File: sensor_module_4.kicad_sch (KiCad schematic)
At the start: 26 parts, among them J1 Conn_Coaxial, J3 Conn_Coaxial, J4 Conn_Coaxial, J5 Conn_Coaxial, U12 REF3025, U13 MCP3204, U16 INA333xxDGK, U17 INA333xxDGK, U18 INA333xxDGK, U19 INA333xxDGK, U6 M24C02-WMN, U7 TPS22929D, U8 REF3040

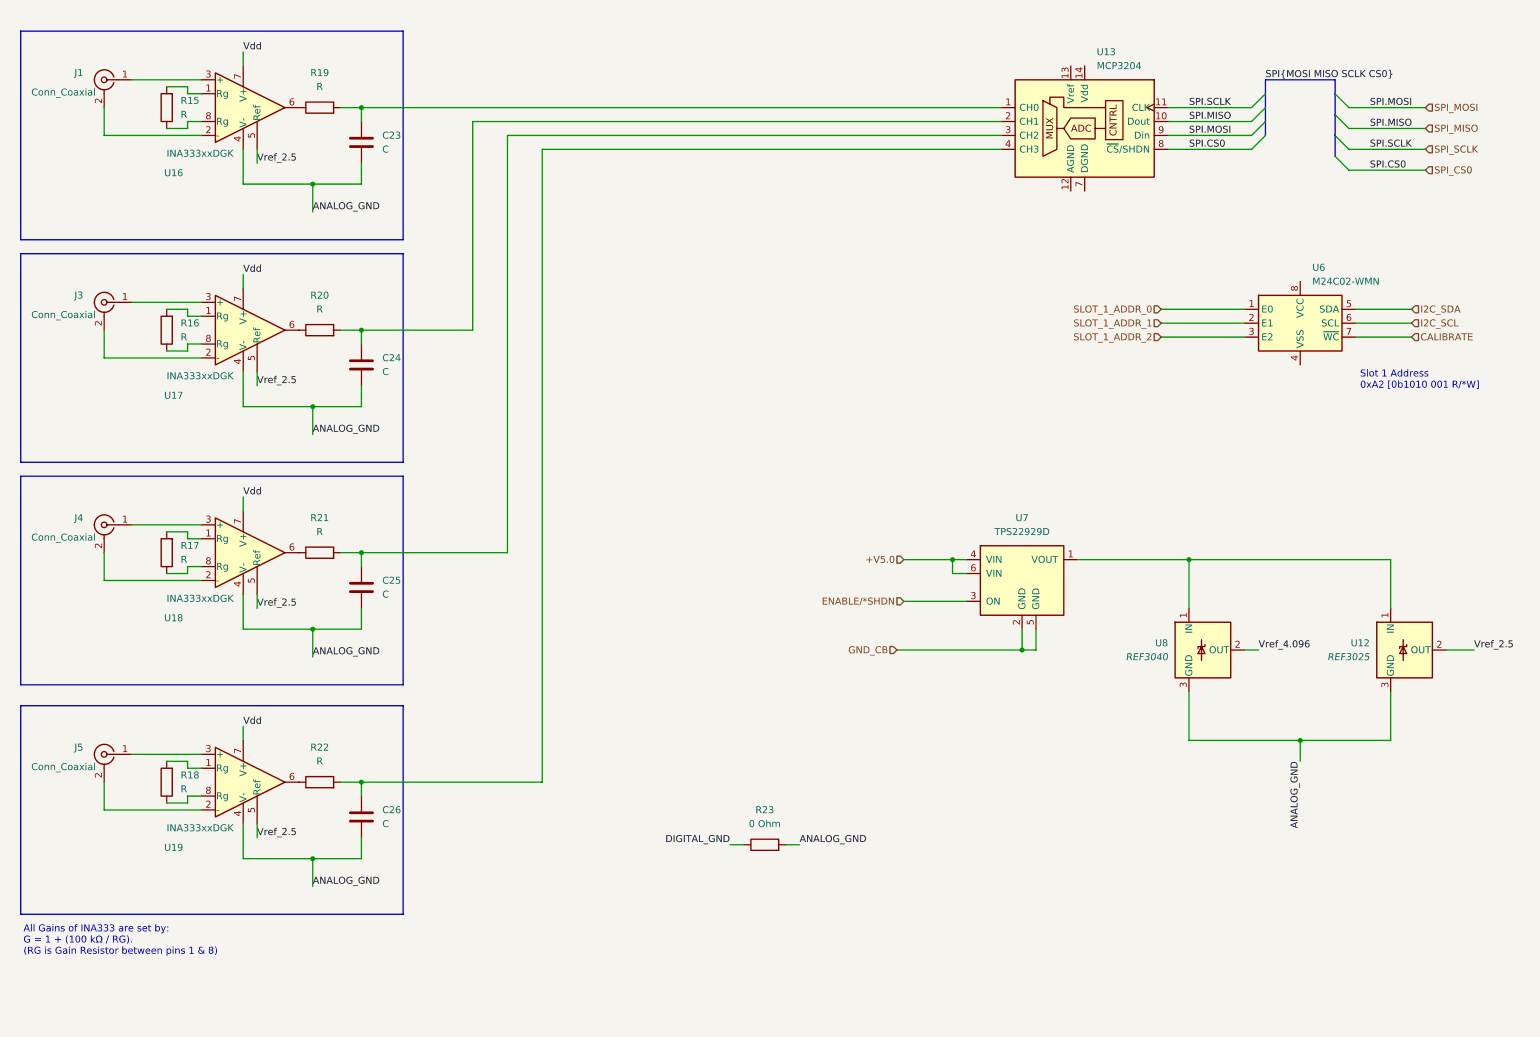
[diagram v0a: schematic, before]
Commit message: Split the sensor modules into a 4 and 8 port version. Fleshed out the power module a bit more. Started adding sensor board connectors to the root schematic and started pulling out sensor boards to their own, separate module. Began wiring up the root schematic to get my bearings a bit.
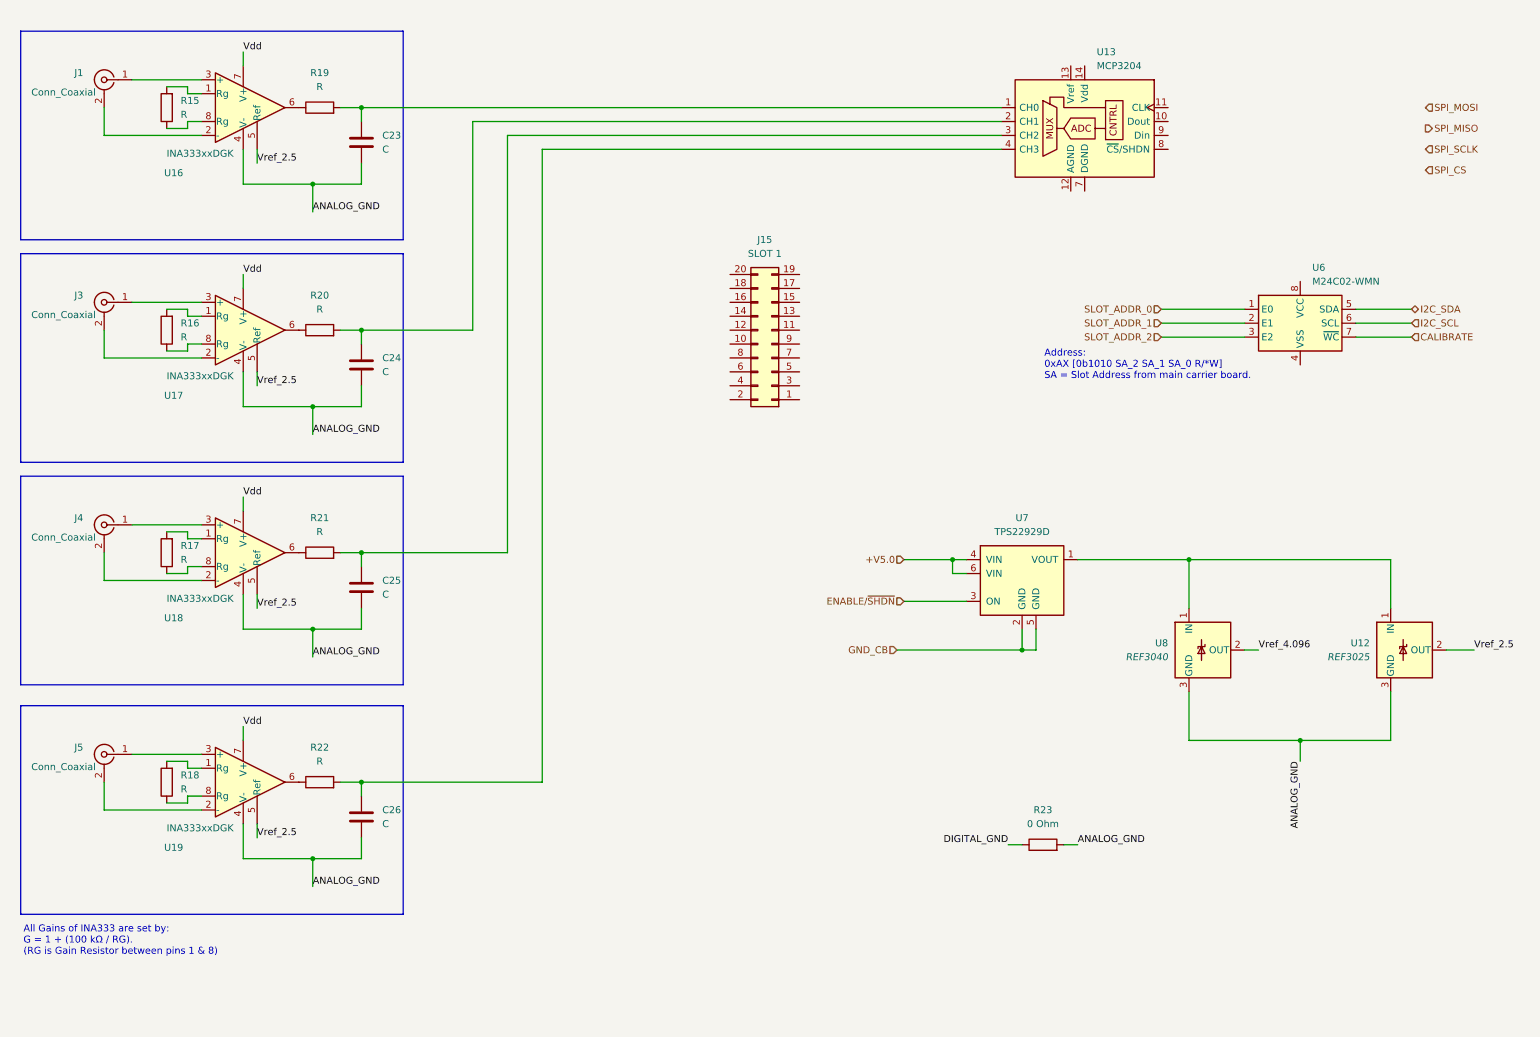
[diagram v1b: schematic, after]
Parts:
- added J15: SLOT 1, symbol Connector_Generic:Conn_02x10_Odd_Even
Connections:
- net SPI_MISO: no longer U13.10 (Dout)
- net SPI_MOSI: no longer U13.9 (Din)
- net SPI_SCLK: no longer U13.11 (CLK)
- net ENABLE/*SHDN renamed ENABLE/~{SHDN}
- net SLOT_1_ADDR_0 renamed SLOT_ADDR_0
- net SLOT_1_ADDR_1 renamed SLOT_ADDR_1
- net SLOT_1_ADDR_2 renamed SLOT_ADDR_2
- net SPI_CS0: no longer names the net of U13.8 (~{CS}/SHDN)
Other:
- note added: "Address: 0xAX [0b1010 SA_2 SA_1 SA_0 R/*W] SA = Slot Address from main carrier board."
- note removed: "Slot 1 Address 0xA2 [0b1010 001 R/*W]"
- moved on the sheet: R23

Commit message: Removed hierarchical labels on the sensor board (4 slot) in favour of local labels and connectors. The idea was that the sensor boards are plug-ins so having them defined as separate boards makes more sense. Eventually I think we'll pull them out of the main schematic and design each one separately with the common connector pinout.
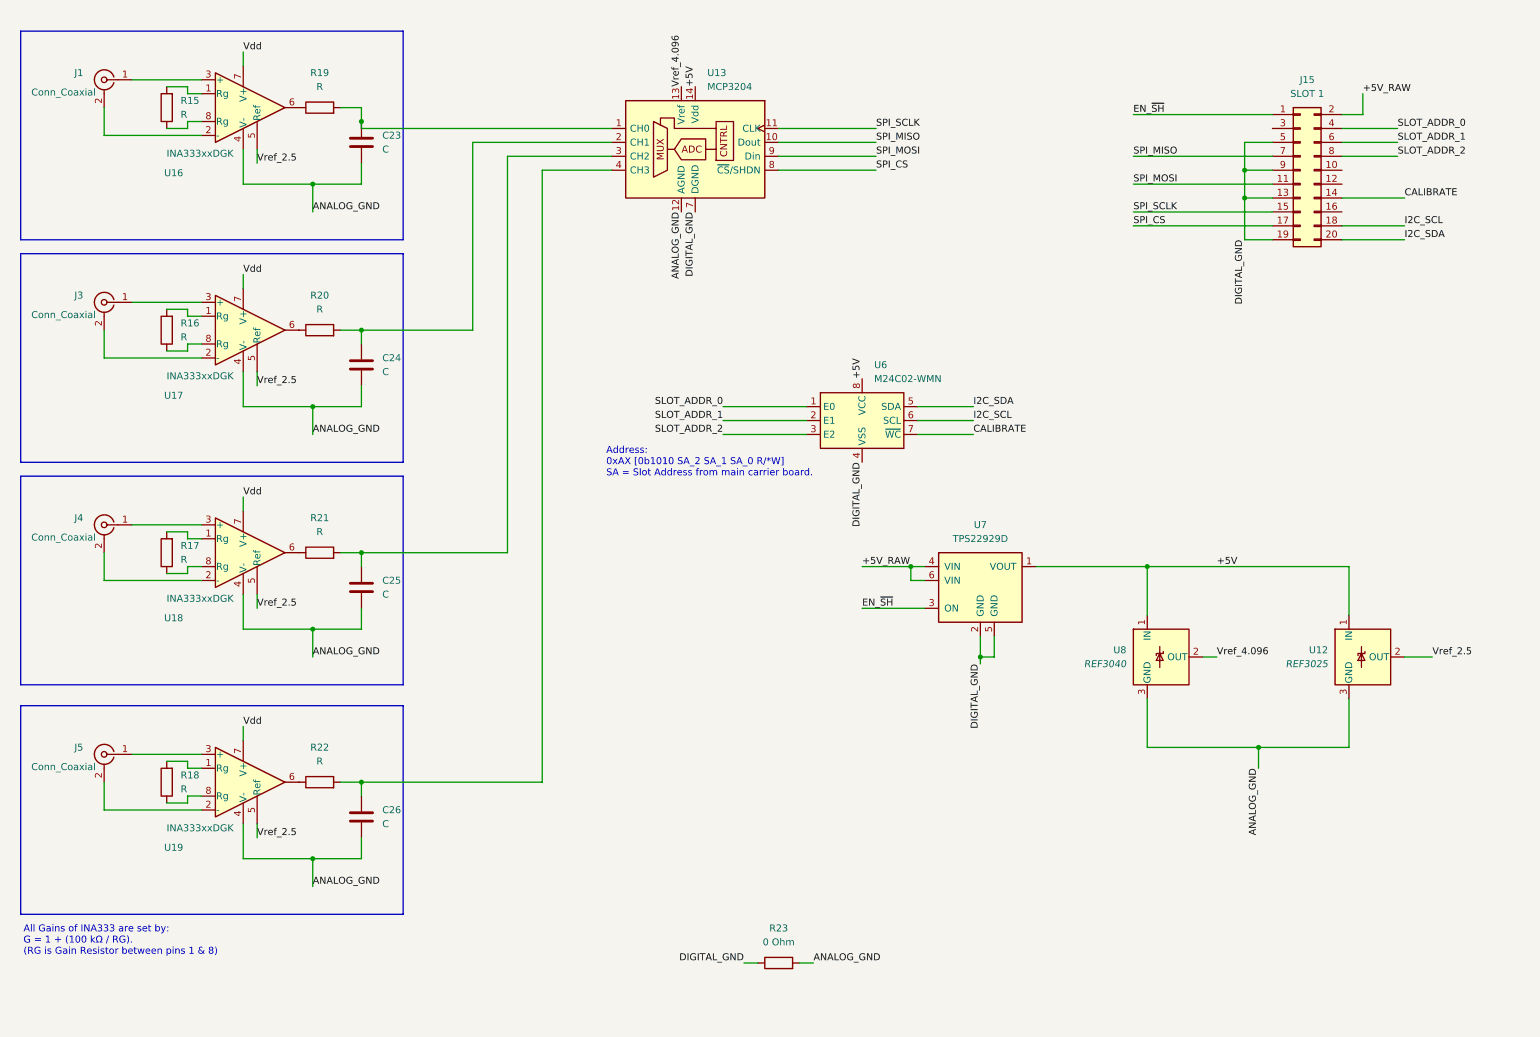
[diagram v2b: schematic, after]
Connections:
- net +V5.0 is gone; now on net +5V_RAW: U7.4 (VIN), U7.6 (VIN)
- net ENABLE/~{SHDN} is gone; now on net EN_~{SH}: U7.3 (ON)
- net GND_CB is gone; now on net DIGITAL_GND: U7.2 (GND), U7.5 (GND)
- net ANALOG_GND: now also U13.12 (AGND)
- net CALIBRATE: now also J15.14 (Pin_14)
- net DIGITAL_GND: now also J15.13 (Pin_13), J15.19 (Pin_19), J15.5 (Pin_5), J15.9 (Pin_9), U13.7 (DGND), U6.4 (VSS)
- net I2C_SCL: now also J15.18 (Pin_18)
- net I2C_SDA: now also J15.20 (Pin_20)
- net SLOT_ADDR_0: now also J15.4 (Pin_4)
- net SLOT_ADDR_1: now also J15.6 (Pin_6)
- net SLOT_ADDR_2: now also J15.8 (Pin_8)
- net SPI_CS: now also J15.17 (Pin_17), U13.8 (~{CS}/SHDN)
- net SPI_MISO: now also J15.7 (Pin_7), U13.10 (Dout)
- net SPI_MOSI: now also J15.11 (Pin_11), U13.9 (Din)
- net SPI_SCLK: now also J15.15 (Pin_15), U13.11 (CLK)
- net Vref_4.096: now also U13.13 (Vref)
- net +5V: now reaches U12.1 (IN), U7.1 (VOUT), U8.1 (IN)
- net +5V: now also U13.14 (Vdd), U6.8 (VCC)
- net EN_~{SH}: now reaches J15.1 (Pin_1)
- net +5V_RAW: now reaches J15.2 (Pin_2)
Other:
- moved on the sheet: J15, R23, U12, U13, U6, U7, U8

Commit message: Cleaned up some signal lines in the sensor board. Shuffled the decoupling caps around a bit as well as rearranged the EEPROM and power supply for clarity. Added buffered 2.5V offset to the pH and ORP circuits. Swapped one TBD input on the base sensor and sensor_4 boards for an ADC calibration input.
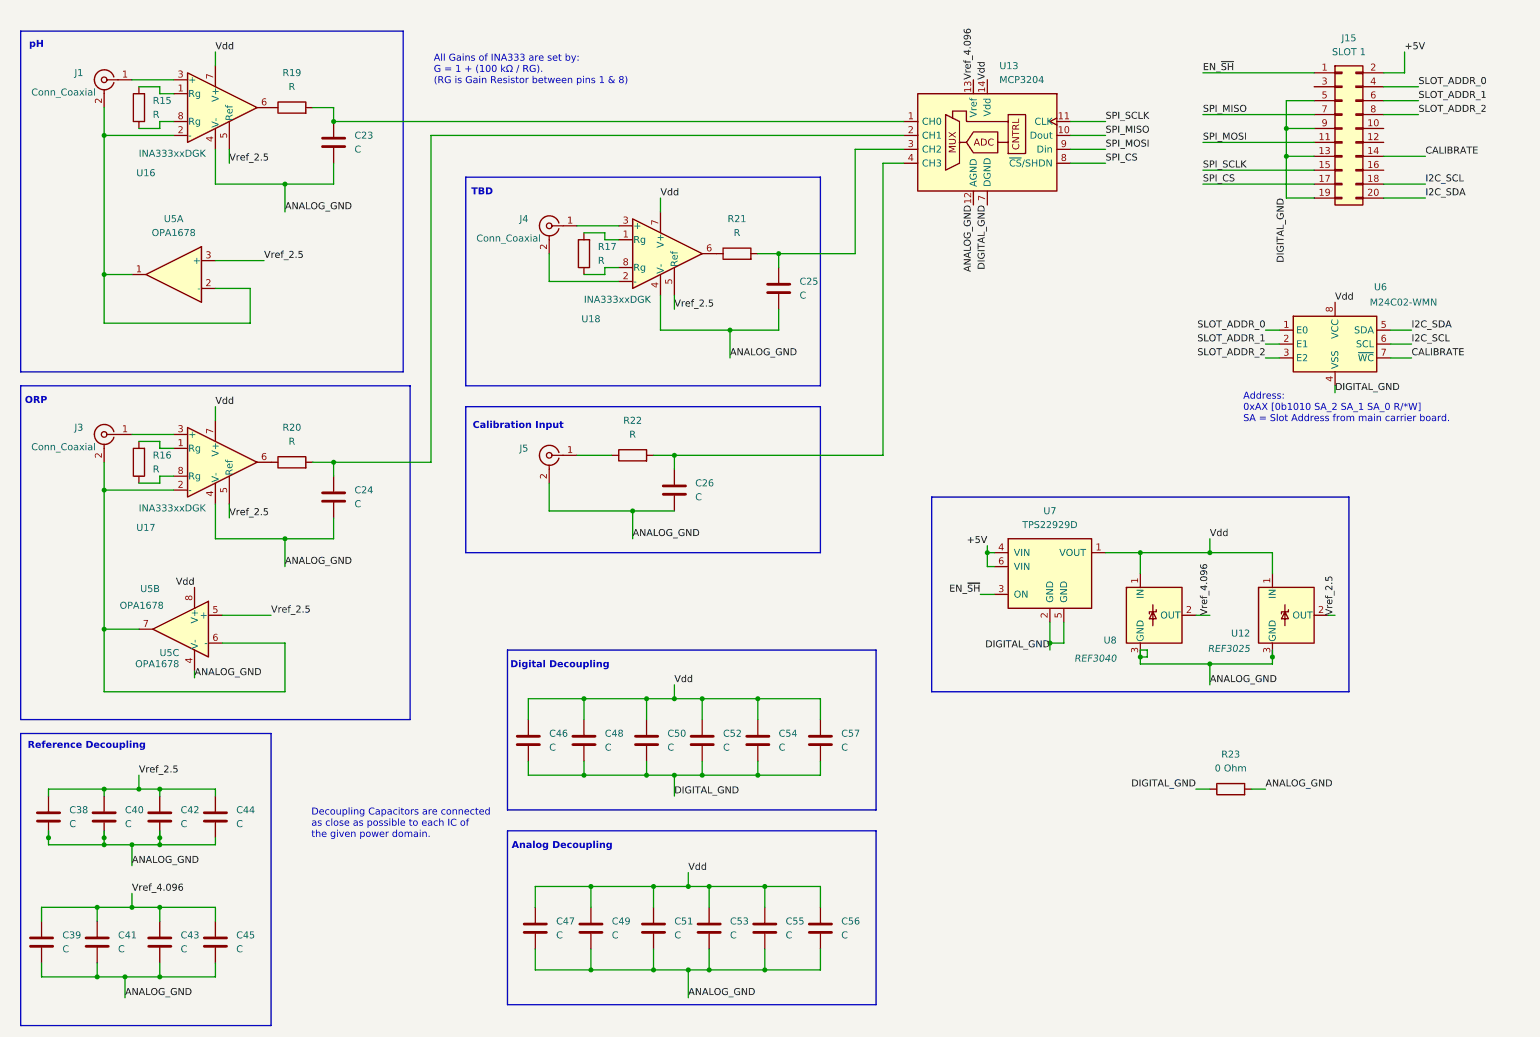
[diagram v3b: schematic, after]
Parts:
- removed R18: R, symbol Device:R
- removed U19: INA333xxDGK, Package_SO:VSSOP-8_3x3mm_P0.65mm, symbol Amplifier_Instrumentation:INA333xxDGK
- added C38, C39, C40, C41, C42, C43, C44, C45, C46, C47, C48, C49, C50, C51, C52, C53, C54, C55, C56, C57: C, symbol Device:C
- added U5: OPA1678, symbol Amplifier_Operational:OPA1678
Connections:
- net +5V_RAW is gone; now on net +5V: J15.2 (Pin_2), U7.4 (VIN), U7.6 (VIN)
- net +5V: no longer U12.1 (IN), U13.14 (Vdd), U6.8 (VCC), U7.1 (VOUT), U8.1 (IN)
- net ANALOG_GND: now also J5.2 (Ext), C38.2, C39.2, C40.2, C41.2, C42.2, C43.2, C44.2, C45.2, C47.2, C49.2, C51.2, C53.2, C55.2, C56.2, U5.4 (V-)
- net DIGITAL_GND: now also C46.2, C48.2, C50.2, C52.2, C54.2, C57.2
- net Vdd: now also U12.1 (IN), U13.14 (Vdd), U6.8 (VCC), U7.1 (VOUT), U8.1 (IN), C46.1, C47.1, C48.1, C49.1, C50.1, C51.1, C52.1, C53.1, C54.1, C55.1, C56.1, C57.1, U5.8 (V+)
- net Vref_2.5: now also C38.1, C40.1, C42.1, C44.1, U5.3 (+), U5.5 (+)
- net Vref_4.096: now also C39.1, C41.1, C43.1, C45.1
- net at J5.1 (In): now also R22.1
- net at J1.2 (Ext), U16.2 (-): now also U5.1, U5.2 (-)
- net at J3.2 (Ext), U17.2 (-): now also U5.6 (-), U5.7
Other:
- note added: "Analog Decoupling"
- note added: "Calibration Input"
- note added: "Decoupling Capacitors are connected as close as possible to each IC of the given power domain."
- note added: "Digital Decoupling"
- note added: "ORP"
- note added: "Reference Decoupling"
- note added: "TBD"
- note added: "pH"
- moved on the sheet: C23, C24, C25, C26, J15, J3, J4, J5, R15, R16, R17, R19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

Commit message: Added some notes to otherwise blank pages. Added the full 8 sensor buffers to the 8 sensor analog board. Added a decoupling sub page to same. Changed a couple of sensor labels on base and 4 board just as placeholders
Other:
- note added: "Turbidity"
- note removed: "TBD"
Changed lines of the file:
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@@
 		)
 	)
-	(text "TBD"
+	(text "Turbidity"
 		(exclude_from_sim no)
 		(at 96.266 43.434 0)
